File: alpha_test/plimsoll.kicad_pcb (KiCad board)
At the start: 4 copper layers, 20 x 50 mm, 46 parts, among them J1 TAG CONNECT, J2 USB_C, J3 Loadd Cell, J4 Test Points, SW1 RESET, SW2 BOOT0, U1 USBLC6-2SC6, U2 APX803L20-29SA-7, U3 STM32F072RBTx, U4 AP2205-3.3, U5 RS3236-3.3, U6 HX717

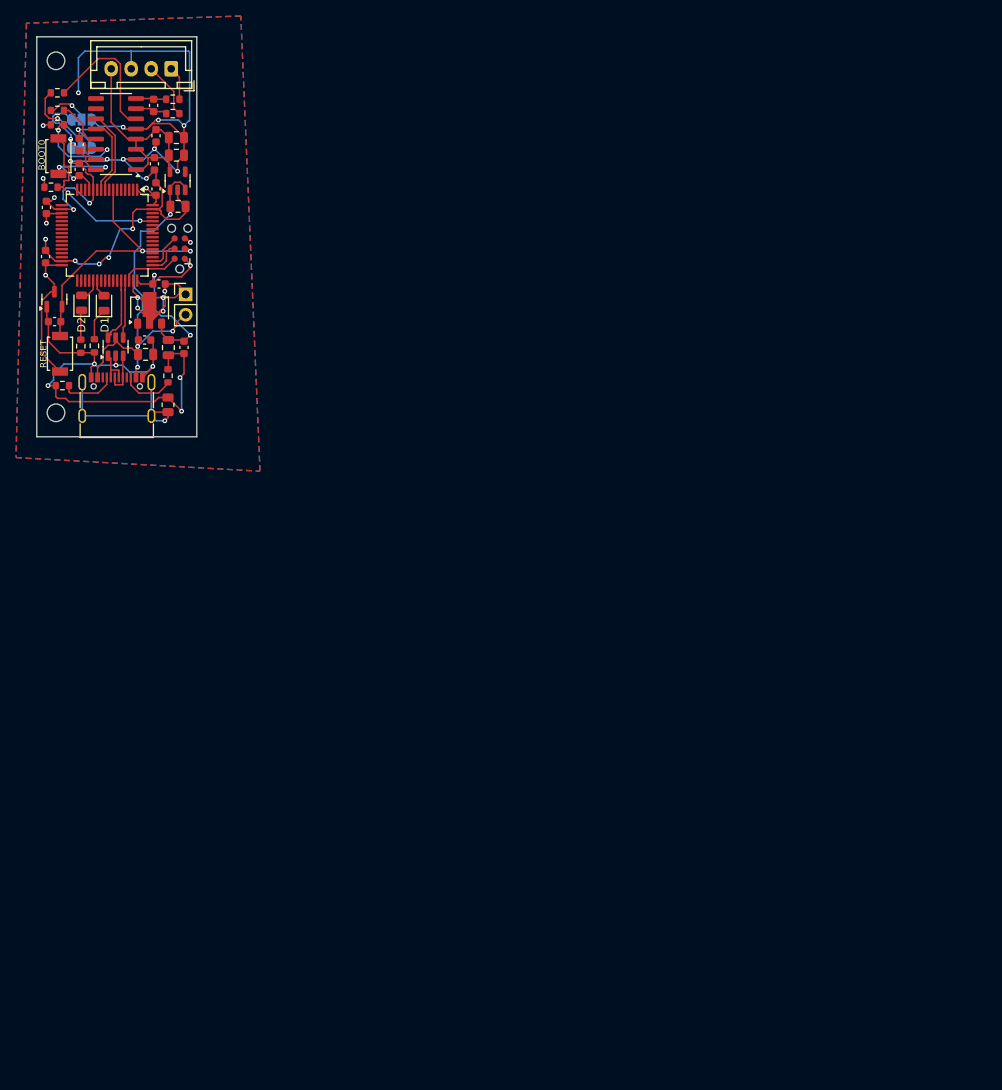
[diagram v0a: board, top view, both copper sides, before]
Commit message: updated alpha test for pcb to reuse parts from the alpha test
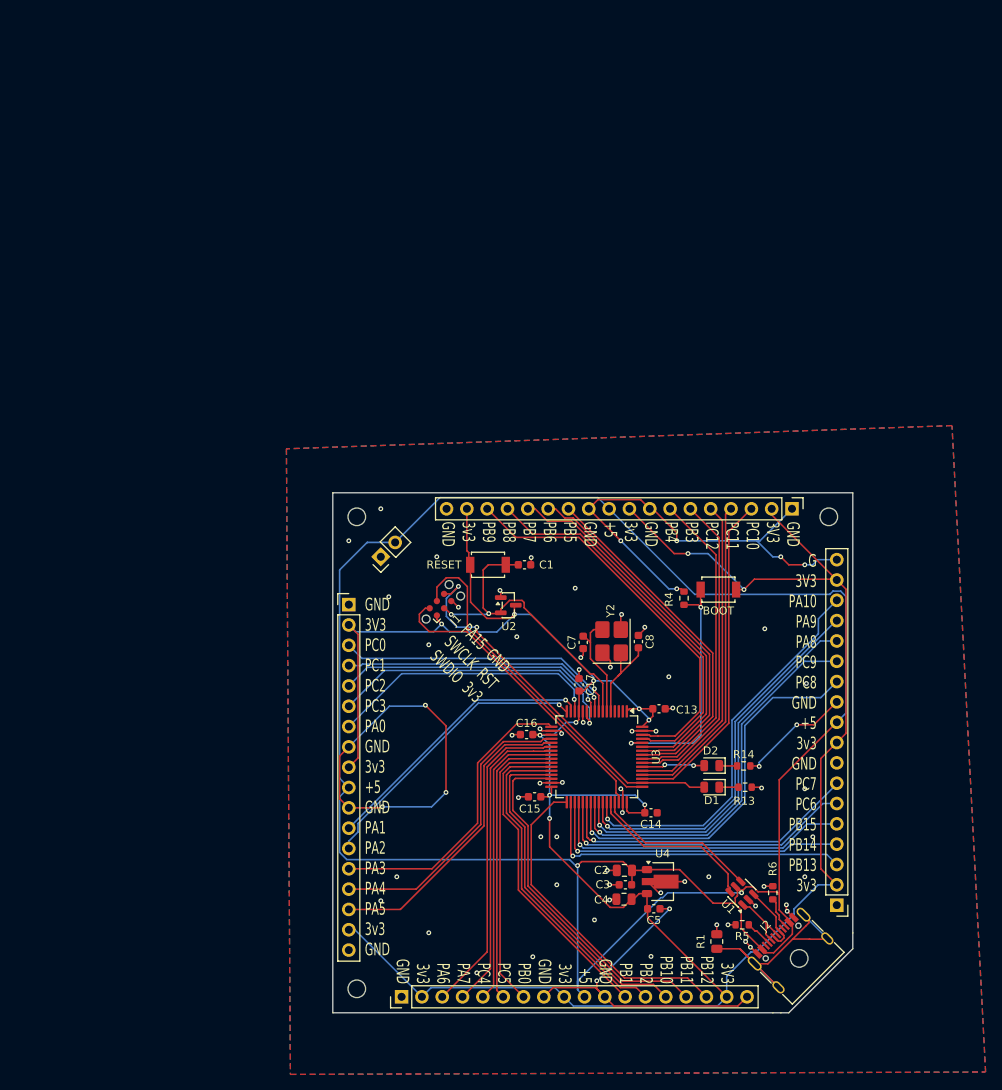
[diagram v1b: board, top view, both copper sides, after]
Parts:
- removed C10, C6: 1u, Capacitor_SMD:C_0805_2012Metric
- removed C11: 10u, Capacitor_SMD:C_0805_2012Metric
- removed C12, C9: 100n, Capacitor_SMD:C_0603_1608Metric
- removed JP1: S0, Jumper:SolderJumper-3_P1.3mm_Bridged12_RoundedPad1.0x1.5mm_NumberLabels
- removed JP2: S1, Jumper:SolderJumper-3_P1.3mm_Bridged12_RoundedPad1.0x1.5mm_NumberLabels
- removed R10, R11, R12: 10k, Resistor_SMD:R_0603_1608Metric
- removed R7, R8: 100, Resistor_SMD:R_0603_1608Metric
- removed SW1: RESET, plimsoll-Library:push_button
- removed SW2: BOOT0, plimsoll-Library:push_button
- removed U5: RS3236-3.3, Package_TO_SOT_SMD:SOT-23-5
- removed U6: HX717, Package_SO:SOP-16_3.9x9.9mm_P1.27mm
- added BOOT: BOOT0, plimsoll-Library:push_button, F.Cu at (105.2, 89.1)
- added H3: MountingHole, MountingHole:MountingHole_2.2mm_M2_ISO7380, F.Cu at (60.0, 139.0)
- added H4: MountingHole, MountingHole:MountingHole_2.2mm_M2_ISO7380, F.Cu at (115.3, 135.2)
- added J5: Conn_01x18, Connector_PinHeader_2.54mm:PinHeader_1x18_P2.54mm_Vertical, F.Cu at (65.6, 140.0)
- added J6: Conn_01x18, Connector_PinHeader_2.54mm:PinHeader_1x18_P2.54mm_Vertical, F.Cu at (120.0, 128.5)
- added J7: Conn_01x18, Connector_PinHeader_2.54mm:PinHeader_1x18_P2.54mm_Vertical, F.Cu at (114.4, 79.0)
- added RESET: RESET, plimsoll-Library:push_button, F.Cu at (76.4, 86.0)
- added Y2: Crystal_GND24, Crystal:Crystal_SMD_3225-4Pin_3.2x2.5mm_HandSoldering, F.Cu at (91.8, 95.5)
- C7, C8: value 100n -> 20pf
- J3: value Loadd Cell -> Conn_01x18; footprint Connector_JST:JST_XH_B4B-XH-A_1x04_P2.50mm_Vertical -> Connector_PinHeader_2.54mm:PinHeader_1x18_P2.54mm_Vertical
- moved J2 109.3 mm to (115.0, 135.0), turned to 45 degrees
- moved R5 108.5 mm to (108.2, 131.0)
- moved C14 107.6 mm to (96.8, 117.0), turned to 180 degrees
- moved U1 103.9 mm to (108.1, 127.0), turned to 135 degrees
- moved R6 99.5 mm to (112.0, 127.0)
- moved C13 99.0 mm to (97.8, 104.0), turned to 180 degrees
- moved R13 98.3 mm to (108.5, 113.8), turned to 0 degrees
- moved R14 98.1 mm to (108.4, 111.1), turned to 0 degrees
- moved D2 97.7 mm to (104.4, 111.1), turned to 180 degrees
- moved H2 97.5 mm to (119.0, 80.0)
- moved D1 97.1 mm to (104.4, 113.8), turned to 180 degrees
- moved U4 96.2 mm to (98.2, 125.6), turned to 0 degrees
- moved R1 96.0 mm to (105.0, 133.1)
- moved R4 94.3 mm to (100.9, 90.2), turned to -90 degrees
- moved C5 91.5 mm to (97.1, 129.0), turned to 180 degrees
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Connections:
- C7 pad 1: Net-(U6-INA-) -> GND
- C7 pad 2: Net-(U6-INA+) -> Net-(U3-PF1)
- C8 pad 1: +3.3VADC -> GND
- C8 pad 2: GND -> Net-(U3-PF0)
- D1 pad 2: Net-(D1-A) -> /PA15
- D2 pad 2: Net-(D2-A) -> /PD2
- J3 pad 1: /Signal+ -> GND
- J3 pad 2: /Signal- -> +3V3
- J3 pad 3: GND -> /PC0
- J3 pad 4: +3.3VADC -> /PC1
- U3 pad 10: /DOUT -> /PC2
- U3 pad 11: unconnected-(U3-PC3-Pad11) -> /PC3
- U3 pad 14: unconnected-(U3-PA0-Pad14) -> /PA0
- U3 pad 15: unconnected-(U3-PA1-Pad15) -> /PA1
- U3 pad 16: unconnected-(U3-PA2-Pad16) -> /PA2
- U3 pad 17: unconnected-(U3-PA3-Pad17) -> /PA3
- U3 pad 20: unconnected-(U3-PA4-Pad20) -> /PA4
- U3 pad 21: unconnected-(U3-PA5-Pad21) -> /PA5
- U3 pad 22: unconnected-(U3-PA6-Pad22) -> /PA6
- U3 pad 23: unconnected-(U3-PA7-Pad23) -> /PA7
- U3 pad 24: unconnected-(U3-PC4-Pad24) -> /PC4
- U3 pad 25: unconnected-(U3-PC5-Pad25) -> /PC5
- U3 pad 26: unconnected-(U3-PB0-Pad26) -> /PB0
- U3 pad 27: unconnected-(U3-PB1-Pad27) -> /PB1
- U3 pad 28: unconnected-(U3-PB2-Pad28) -> /PB2
- U3 pad 29: unconnected-(U3-PB10-Pad29) -> /PB10
- U3 pad 30: unconnected-(U3-PB11-Pad30) -> /PB11
- U3 pad 33: unconnected-(U3-PB12-Pad33) -> /PB12
- U3 pad 34: unconnected-(U3-PB13-Pad34) -> /PB13
- U3 pad 35: unconnected-(U3-PB14-Pad35) -> /PB14
- U3 pad 36: unconnected-(U3-PB15-Pad36) -> /PB15
- U3 pad 37: Net-(D2-A) -> /PC6
- U3 pad 38: Net-(D1-A) -> /PC7
- U3 pad 39: unconnected-(U3-PC8-Pad39) -> /PC8
- U3 pad 40: unconnected-(U3-PC9-Pad40) -> /PC9
- U3 pad 41: unconnected-(U3-PA8-Pad41) -> /PA8
- U3 pad 42: unconnected-(U3-PA9-Pad42) -> /PA9
- U3 pad 43: unconnected-(U3-PA10-Pad43) -> /PA10
- U3 pad 5: unconnected-(U3-PF0-Pad5) -> Net-(U3-PF0)
- U3 pad 51: unconnected-(U3-PC10-Pad51) -> /PC10
- U3 pad 52: unconnected-(U3-PC11-Pad52) -> /PC11
- U3 pad 53: unconnected-(U3-PC12-Pad53) -> /PC12
- U3 pad 54: unconnected-(U3-PD2-Pad54) -> /PD2
- U3 pad 55: unconnected-(U3-PB3-Pad55) -> /PB3
- U3 pad 56: unconnected-(U3-PB4-Pad56) -> /PB4
- U3 pad 57: unconnected-(U3-PB5-Pad57) -> /PB5
- U3 pad 58: unconnected-(U3-PB6-Pad58) -> /PB6
- U3 pad 59: unconnected-(U3-PB7-Pad59) -> /PB7
- U3 pad 6: unconnected-(U3-PF1-Pad6) -> Net-(U3-PF1)
- U3 pad 61: unconnected-(U3-PB8-Pad61) -> /PB8
- U3 pad 62: unconnected-(U3-PB9-Pad62) -> /PB9
- U3 pad 8: unconnected-(U3-PC0-Pad8) -> /PC0
- U3 pad 9: /PD_SCK -> /PC1
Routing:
- net +3V3: track 80.1 -> 332.3 mm, vias 10 -> 12
- net VBUS: track 52.6 -> 274.1 mm, vias 4 -> 2
- net /PA10: track 0.00 -> 49.5 mm, vias 0 -> 1
- net /PB9: track 0.00 -> 49.5 mm
- net /PC8: track 0.00 -> 48.5 mm, vias 0 -> 1
- net /PC9: track 0.00 -> 48.5 mm, vias 0 -> 1
- net /PA9: track 0.00 -> 48.4 mm, vias 0 -> 1
- net /PA8: track 0.00 -> 48.4 mm, vias 0 -> 1
- net /PB8: track 0.00 -> 48.2 mm
- net /PB7: track 0.00 -> 46.9 mm
- net /PB6: track 0.00 -> 45.6 mm
- net /PB11: track 0.00 -> 44.4 mm
- net /PB5: track 0.00 -> 44.2 mm
- net /PA15: track 4.56 -> 48.0 mm, vias 0 -> 2
- net /PB10: track 0.00 -> 43.3 mm
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- added copper zone on In1.Cu, net GND
- removed copper zone on In1.Cu, net +3V3
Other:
- board size 20 x 50 mm -> 65 x 65 mm
- board text added: "+5 GND"
- board text added: "3V3 PB12 PB11 PB10 PB2 PB1 GND +5 3v3 GND PB0 PC5 PC4 PA7 PA6 3v3 GND"
- board text added: "G 3V3 PA10 PA9 PA8 PC9 PC8 GND +5 3v3 GND PC7 PC6 PB15 PB14 PB13 3v3"
- board text added: "G 3V3 PA10 PA9 PA8 PC9 PC8 GND +5 3v3 GND PC7 PC6 PB15 PB14 PB13 3v3 GND"
- board text added: "G 3V3 PB12 PB11 PB10 PB2 PB1 GND +5 3v3 GND PB0 PC5 PC4 PA7 PA6 3v3 G"
- board text added: "GND 3V3 PC0 PC1 PC2 PC3 PA0 GND 3v3 +5 GND PA1 PA2 PA3 PA4 PA5 3v3 GND"
- board text added: "GND 3V3 PC10 PC11 PC12 PB3 PB4 GND 3v3 +5 GND PB5 PB6 PB7 PB8 PB9 3v3 GND"
- board text added: "PA15 GND SWCLK RST SWDIO 3v3"
- board text removed: "BOOT0"
- board text removed: "GND Vbus"
- board text removed: "PCB Revision 0"
- board text removed: "RESET"
- board text removed: "S+ S- E- E+"
- board text removed: "S0"
- board text removed: "S1"
- board text removed: "https://github.com/mulcmu/plimsoll"
